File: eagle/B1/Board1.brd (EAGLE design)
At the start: 101.6 x 53.3 mm, 18 parts

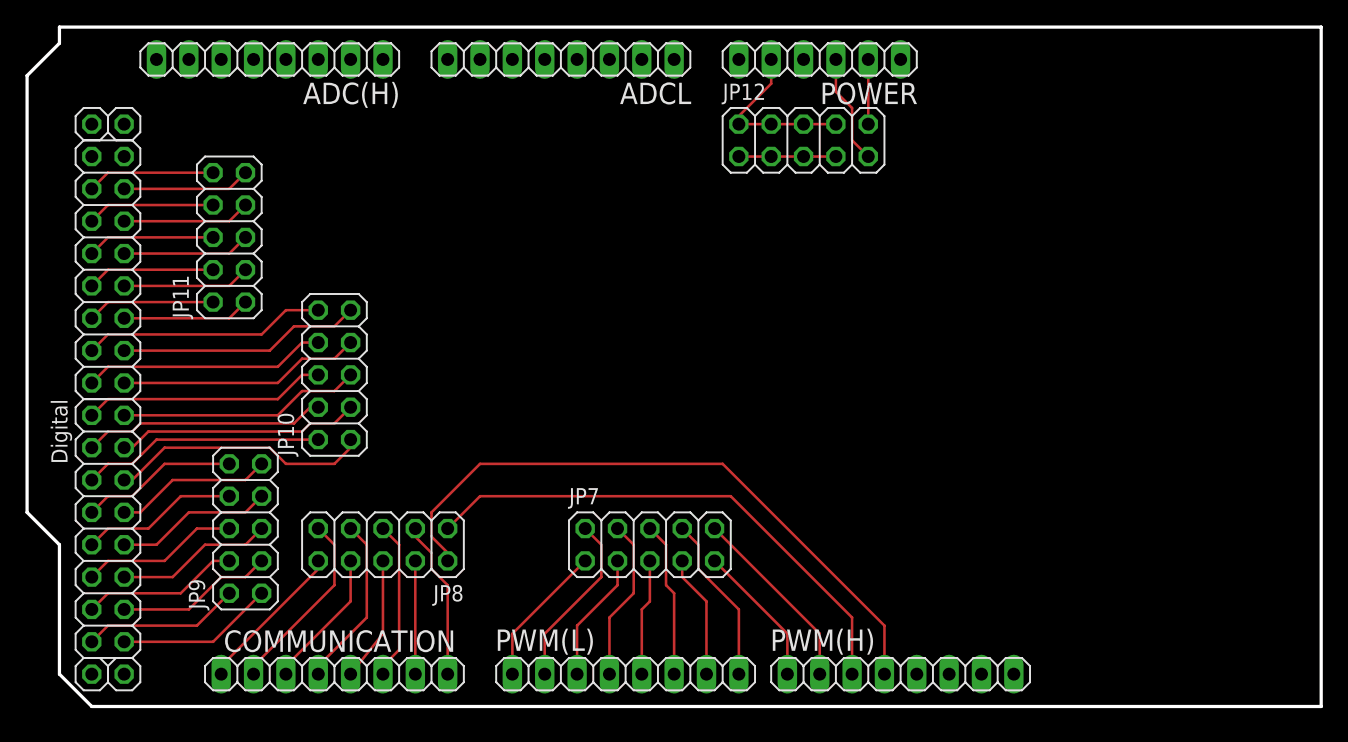
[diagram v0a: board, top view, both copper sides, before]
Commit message: Redesign board 1 (non-LED board)
This contains 3 major changes:

* Pins 0 and 1 (TX/RX) are no longer used as data pins
* SMD components are used for the 2x5 headers
* 3.3v and 5v power breakouts are dropped in favor of making the 2x5 GND
connection be omnidirectional
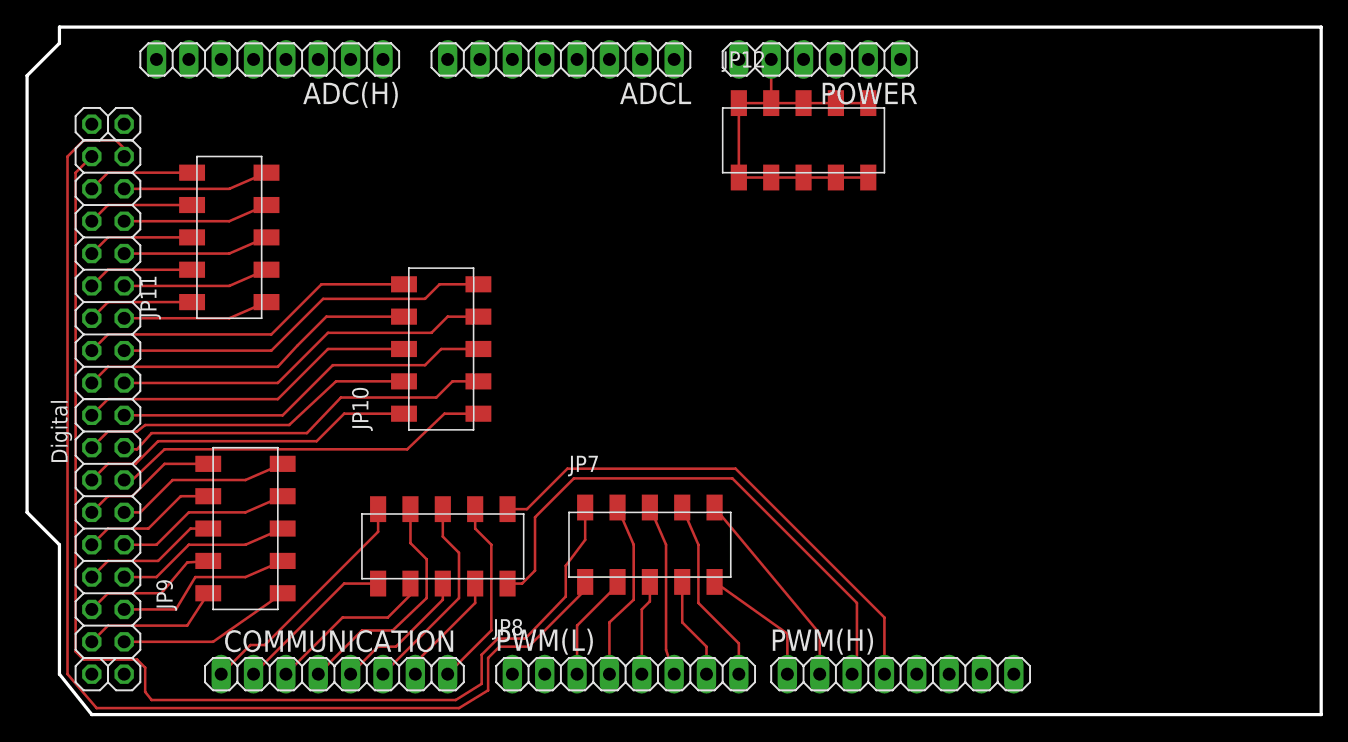
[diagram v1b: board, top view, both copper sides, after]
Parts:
- JP10, JP11, JP12, JP7, JP8, JP9: device pinhead:2X05 -> pinhead+:2X05_SMT
- moved JP10 8.62 mm to (32.5, 28.1)
- moved JP8 4.70 mm to (32.6, 12.6)
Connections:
- removed net PWM00: JP7.1, PWM(L).1
- removed net PWM01: JP7.2, PWM(L).2
- removed net SCL_D21: COMMUNICATION.1, JP8.10
- new net N$1: COMMUNICATION.2, JP8.10
- net +3V3: no longer JP12.10
- net +5V: no longer JP12.9
- net DIG52: now also JP7.1
- net DIG53: now also JP7.2
- net GND: now also JP12.10, JP12.9
- net PWM10: now also PWM(H).4; no longer PWM(H).3
- net PWM11: now also PWM(H).3; no longer PWM(H).4
- net SDA_D20: now also COMMUNICATION.1; no longer COMMUNICATION.2
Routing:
- net DIG52: track 0.00 -> 94.2 mm
- net DIG53: track 0.00 -> 92.7 mm
- net PWM01: track 13.8 -> 0.00 mm
- net N$1: track 0.00 -> 12.7 mm
- net SCL_D21: track 12.0 -> 0.00 mm
- net PWM00: track 11.3 -> 0.00 mm
- net DIG34: track 19.1 -> 30.2 mm
- net DIG38: track 19.1 -> 30.0 mm
- net DIG36: track 19.1 -> 30.0 mm
- net DIG40: track 19.1 -> 30.0 mm
- net DIG32: track 20.5 -> 29.9 mm
- net +5V: track 8.67 -> 0.00 mm
- net GND: track 21.4 -> 30.0 mm
- net DIG39: track 19.1 -> 26.7 mm
- net DIG41: track 19.1 -> 26.7 mm
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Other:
- board size 101.6 x 53.3 mm -> 101.6 x 54 mm
